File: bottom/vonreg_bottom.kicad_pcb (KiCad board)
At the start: 2 copper layers, 68.6 x 83.6 mm, 8 parts, among them J1 AudioJack4, T1 SW_Push, T2 SW_Push, T3 SW_Push

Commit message: Routing done, hopefully
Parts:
- J1: footprint keebio:TRRS-PJ-320A-dual -> Connector_Audio:TRRS-PJ-320A-dual
- T1, T2, T3: footprint Button_Switch_Keyboard:SW_Cherry_MX_1.00u_PCB -> Button_Switch_Keyboard:Kailh_socket_MX_optional_reversible
- moved T3 5.12 mm to (101.1, 108.3)
- moved T1 5.12 mm to (61.1, 108.3)
- moved T2 5.12 mm to (81.1, 108.3)
- moved J1 0.85 mm to (77.0, 37.2)
- moved BlackPill_reversed1 0.18 mm to (63.1, 38.0)
- gave numbers to parts that had none: 2
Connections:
- BlackPill1 pad 1: K1 -> K14
- BlackPill1 pad 11: K6 -> K2
- BlackPill1 pad 12: K7 -> K15
- BlackPill1 pad 13: K8 -> K9
- BlackPill1 pad 14: K9 -> K12
- BlackPill1 pad 15: K10 -> T3
- BlackPill1 pad 16: K11 -> T2
- BlackPill1 pad 17: K12 -> T1
- BlackPill1 pad 2: K2 -> K13
- BlackPill1 pad 20: 3V3 -> unconnected-(BlackPill1-Pad20)
- BlackPill1 pad 28: TX1 -> K6
- BlackPill1 pad 3: K3 -> TX1
- BlackPill1 pad 30: T3 -> K3
- BlackPill1 pad 31: T2 -> K8
- BlackPill1 pad 32: T1 -> K11
- BlackPill1 pad 33: K15 -> K7
- BlackPill1 pad 34: K14 -> K10
- BlackPill1 pad 35: K13 -> K4
- BlackPill1 pad 4: K4 -> K1
- BlackPill_reversed1 pad 1: K1 -> K14
- BlackPill_reversed1 pad 11: K6 -> K2
- BlackPill_reversed1 pad 12: K7 -> K15
- BlackPill_reversed1 pad 13: K8 -> K9
- BlackPill_reversed1 pad 14: K9 -> K12
- BlackPill_reversed1 pad 15: K10 -> T3
- BlackPill_reversed1 pad 16: K11 -> T2
- BlackPill_reversed1 pad 17: K12 -> T1
- BlackPill_reversed1 pad 2: K2 -> K13
- BlackPill_reversed1 pad 20: 3V3 -> unconnected-(BlackPill_reversed1-Pad20)
- BlackPill_reversed1 pad 28: TX1 -> K6
- BlackPill_reversed1 pad 3: K3 -> TX1
- BlackPill_reversed1 pad 30: T3 -> K3
- BlackPill_reversed1 pad 31: T2 -> K8
- BlackPill_reversed1 pad 32: T1 -> K11
- BlackPill_reversed1 pad 33: K15 -> K7
- BlackPill_reversed1 pad 34: K14 -> K10
- BlackPill_reversed1 pad 35: K13 -> K4
- BlackPill_reversed1 pad 4: K4 -> K1
- PinsBottomA1 pad 1: K1 -> unconnected-(PinsBottomA1-Pad1)
- PinsBottomA1 pad 10: K10 -> K7
- PinsBottomA1 pad 2: K2 -> K14
- PinsBottomA1 pad 3: K3 -> unconnected-(PinsBottomA1-Pad3)
- PinsBottomA1 pad 4: K4 -> K13
- PinsBottomA1 pad 5: K5 -> unconnected-(PinsBottomA1-Pad5)
- PinsBottomA1 pad 6: K6 -> K1
- PinsBottomA1 pad 7: K7 -> unconnected-(PinsBottomA1-Pad7)
- PinsBottomA1 pad 8: K8 -> K4
- PinsBottomA1 pad 9: K9 -> K10
- PinsBottomB1 pad 1: K11 -> K8
- PinsBottomB1 pad 10: GND -> K9
- PinsBottomB1 pad 2: K12 -> K11
- PinsBottomB1 pad 3: K13 -> K5
- PinsBottomB1 pad 4: K14 -> GND
- PinsBottomB1 pad 5: K15 -> K2
- PinsBottomB1 pad 6: unconnected-(PinsBottomB1-Pad6) -> K3
- PinsBottomB1 pad 7: unconnected-(PinsBottomB1-Pad7) -> K15
- PinsBottomB1 pad 8: unconnected-(PinsBottomB1-Pad8) -> K6
- PinsBottomB1 pad 9: unconnected-(PinsBottomB1-Pad9) -> K12
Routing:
- net GND: track 0.00 -> 236.2 mm
- net T3: track 0.00 -> 90.1 mm
- net T2: track 0.00 -> 76.0 mm
- net T1: track 0.00 -> 62.7 mm
- net K6: track 0.00 -> 48.8 mm
- net K11: track 0.00 -> 48.7 mm
- net K3: track 0.00 -> 48.7 mm
- net K8: track 0.00 -> 45.4 mm
- net K9: track 0.00 -> 44.1 mm
- net K7: track 0.00 -> 43.7 mm
- net K4: track 0.00 -> 43.2 mm
- net K13: track 0.00 -> 42.3 mm
- net K5: track 0.00 -> 41.6 mm
- net K15: track 0.00 -> 41.5 mm
- net K2: track 0.00 -> 41.5 mm
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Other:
- outline, holes or cut-outs redrawn

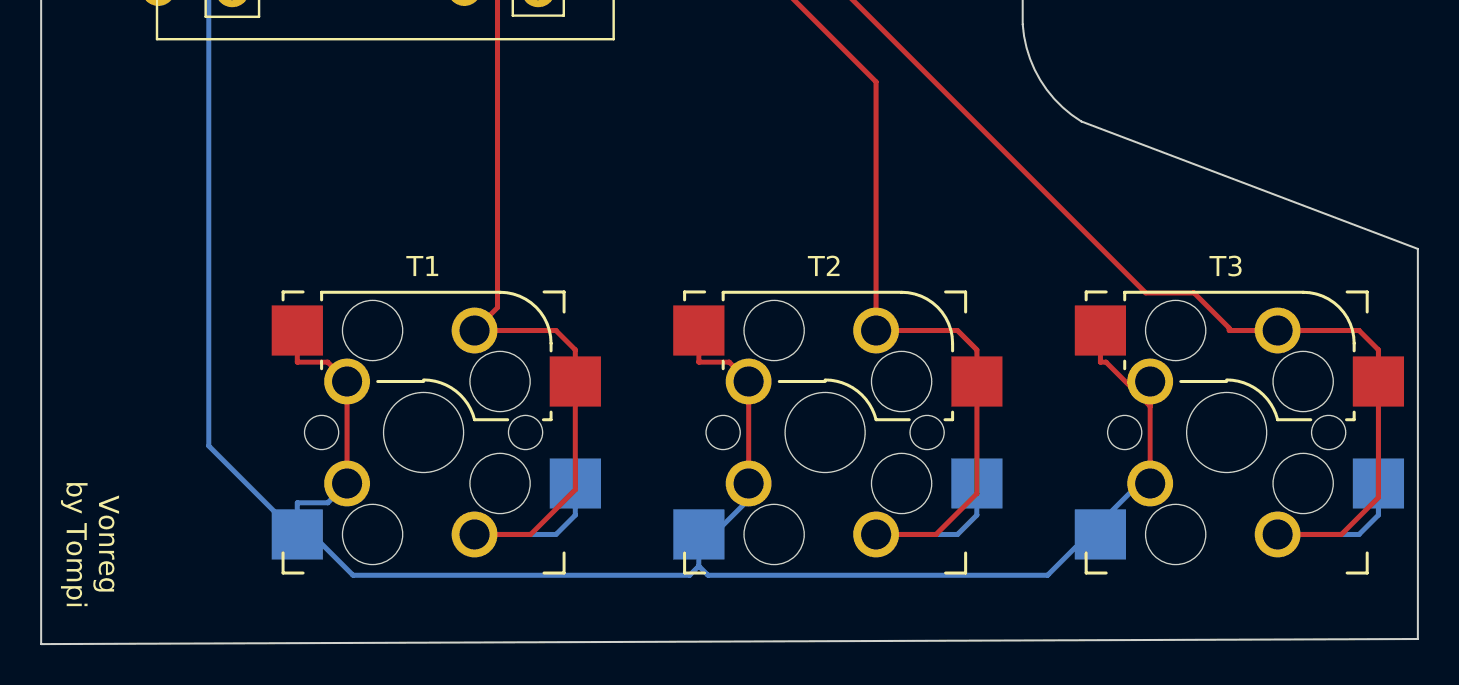
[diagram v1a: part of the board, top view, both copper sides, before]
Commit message: Rounded edge cuts
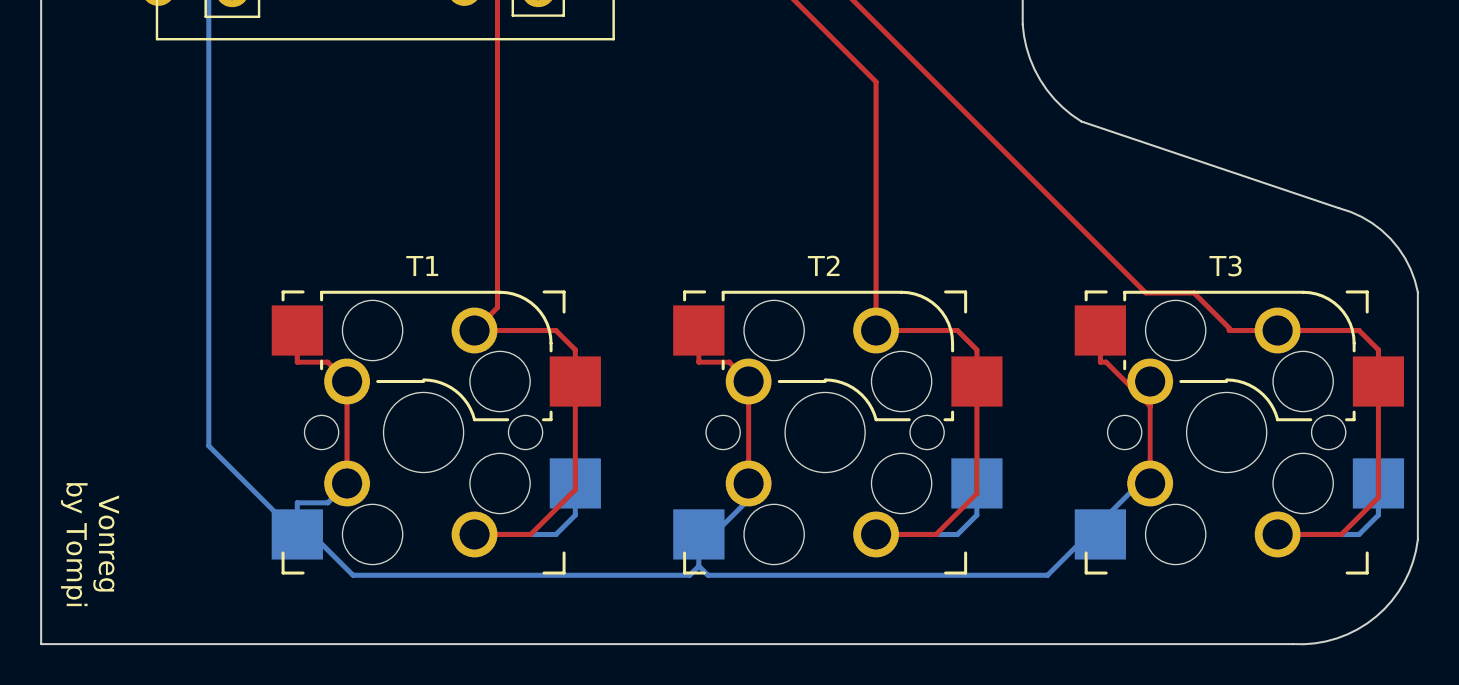
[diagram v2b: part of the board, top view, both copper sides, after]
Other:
- outline, holes or cut-outs redrawn
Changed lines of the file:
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@@
       (outputformat 1)
       (mirror false)
-      (drillshape 1)
+      (drillshape 0)
       (scaleselection 1)
-      (outputdirectory "")
+      (outputdirectory "gerber")
     )
   )
@@
   (gr_line (start 42.037 35.306) (end 84.328 35.306) (layer "Edge.Cuts") (width 0.1))
   (gr_line (start 42.037 118.872) (end 42.037 35.306) (layer "Edge.Cuts") (width 0.1))
-  (gr_line (start 110.617 118.618) (end 42.037 118.872) (layer "Edge.Cuts") (width 0.1))
+  (gr_line (start 104.394 118.872) (end 42.037 118.872) (layer "Edge.Cuts") (width 0.1))
   (gr_line (start 90.932 40.386) (end 90.932 88) (layer "Edge.Cuts") (width 0.1))
-  (gr_line (start 110.617 99.187) (end 110.617 118.618) (layer "Edge.Cuts") (width 0.1))
+  (gr_arc (start 106.68 97.155) (mid 109.256167 98.679662) (end 110.617 101.346) (layer "Edge.Cuts") (width 0.1))
+  (gr_arc (start 110.617 113.665) (mid 108.539478 117.50423) (end 104.394 118.872) (layer "Edge.Cuts") (width 0.1))
+  (gr_line (start 110.617 101.346) (end 110.617 113.665) (layer "Edge.Cuts") (width 0.1))
   (gr_arc (start 93.853 92.837) (mid 91.805949 90.772711) (end 90.932 88) (layer "Edge.Cuts") (width 0.1))
   (gr_arc (start 84.328 35.306) (mid 88.511705 36.699783) (end 90.932 40.386) (layer "Edge.Cuts") (width 0.1))
-  (gr_line (start 93.853 92.837) (end 110.617 99.187) (layer "Edge.Cuts") (width 0.1))
+  (gr_line (start 93.853 92.837) (end 106.68 97.155) (layer "Edge.Cuts") (width 0.1))
   (gr_text "3V3 Here" (at 57.15 83.693) (layer "B.SilkS")
     (effects (font (size 1 1) (thickness 0.15)) (justify mirror))

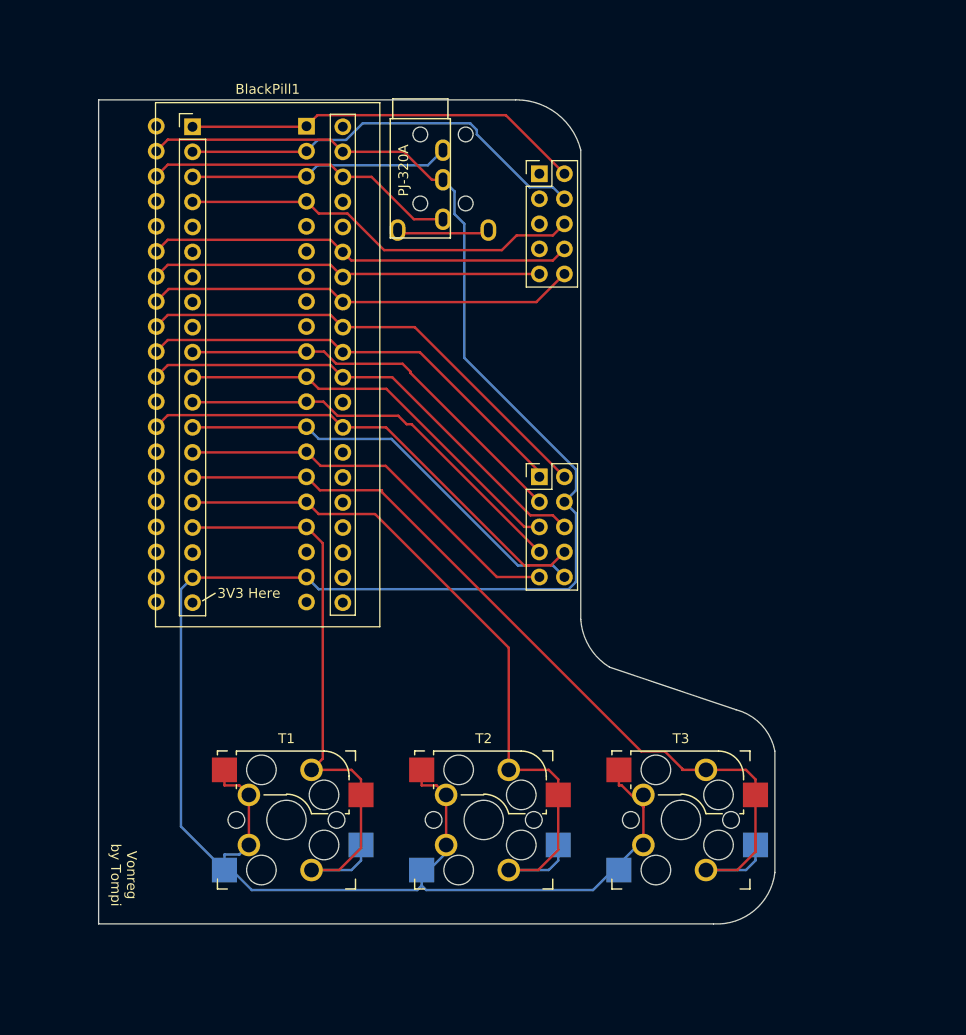
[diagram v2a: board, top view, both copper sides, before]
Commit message: Ground pour and buzzer
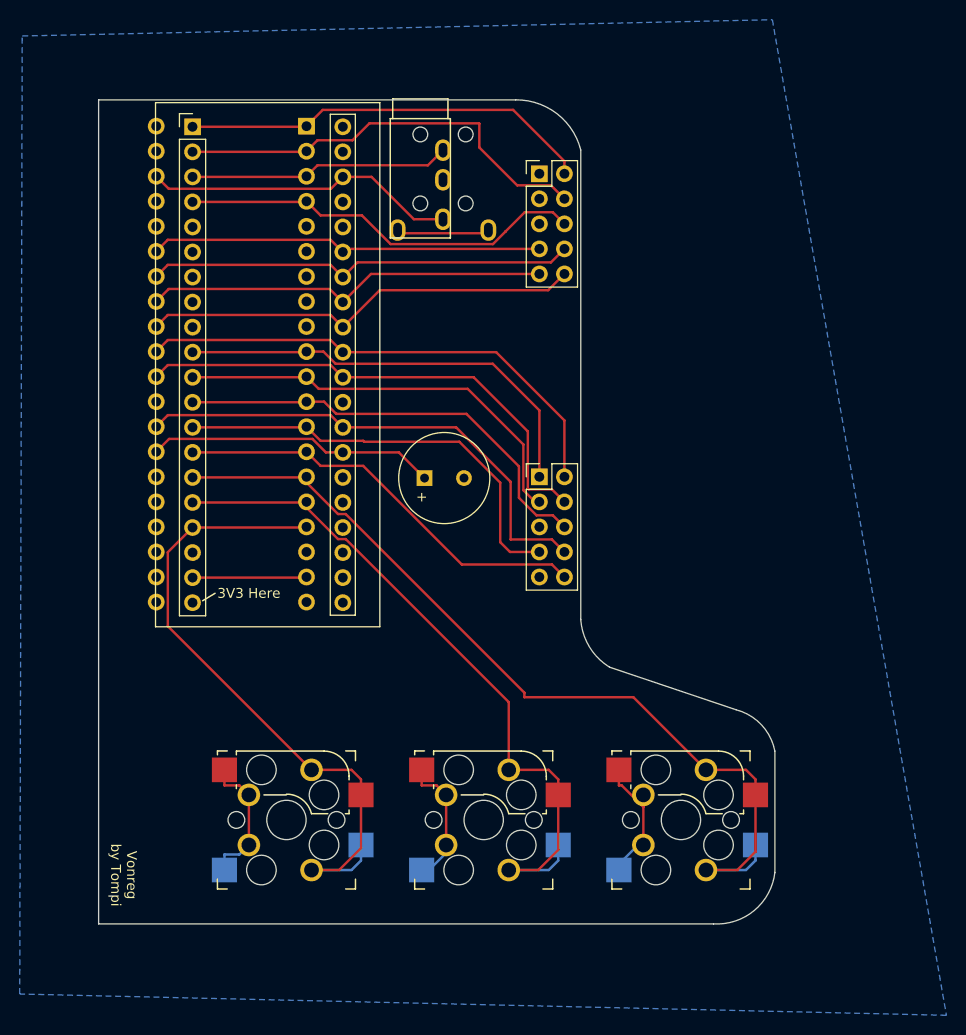
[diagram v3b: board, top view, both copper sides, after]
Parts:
- added BZ1: Buzzer, Buzzer_Beeper:MagneticBuzzer_PUI_AT-0927-TT-6-R, F.Cu at (75.1, 73.7)
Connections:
- BlackPill1 pad 1: K14 -> K1
- BlackPill1 pad 10: K5 -> K2
- BlackPill1 pad 11: K2 -> K8
- BlackPill1 pad 12: K15 -> K12
- BlackPill1 pad 14: K12 -> K3
- BlackPill1 pad 2: K13 -> K4
- BlackPill1 pad 27: unconnected-(BlackPill1-Pad27) -> BUZZER
- BlackPill1 pad 30: K3 -> K15
- BlackPill1 pad 31: K8 -> K5
- BlackPill1 pad 33: K7 -> K14
- BlackPill1 pad 34: K10 -> K13
- BlackPill1 pad 35: K4 -> K10
- BlackPill1 pad 4: K1 -> K7
- BlackPill_reversed1 pad 1: K14 -> K1
- BlackPill_reversed1 pad 10: K5 -> K2
- BlackPill_reversed1 pad 11: K2 -> K8
- BlackPill_reversed1 pad 12: K15 -> K12
- BlackPill_reversed1 pad 14: K12 -> K3
- BlackPill_reversed1 pad 2: K13 -> K4
- BlackPill_reversed1 pad 27: unconnected-(BlackPill_reversed1-Pad27) -> BUZZER
- BlackPill_reversed1 pad 30: K3 -> K15
- BlackPill_reversed1 pad 31: K8 -> K5
- BlackPill_reversed1 pad 33: K7 -> K14
- BlackPill_reversed1 pad 34: K10 -> K13
- BlackPill_reversed1 pad 35: K4 -> K10
- BlackPill_reversed1 pad 4: K1 -> K7
- PinsBottomA1 pad 1: unconnected-(PinsBottomA1-Pad1) -> GND
- PinsBottomA1 pad 10: K7 -> K11
- PinsBottomA1 pad 2: K14 -> K1
- PinsBottomA1 pad 4: K13 -> K4
- PinsBottomA1 pad 6: K1 -> K7
- PinsBottomA1 pad 7: unconnected-(PinsBottomA1-Pad7) -> K10
- PinsBottomA1 pad 8: K4 -> K13
- PinsBottomA1 pad 9: K10 -> K14
- PinsBottomB1 pad 1: K8 -> K2
- PinsBottomB1 pad 10: K9 -> K3
- PinsBottomB1 pad 2: K11 -> K5
- PinsBottomB1 pad 3: K5 -> K8
- PinsBottomB1 pad 4: GND -> K15
- PinsBottomB1 pad 5: K2 -> unconnected-(PinsBottomB1-Pad5)
- PinsBottomB1 pad 6: K3 -> K12
- PinsBottomB1 pad 7: K15 -> K9
- PinsBottomB1 pad 9: K12 -> unconnected-(PinsBottomB1-Pad9)
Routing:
- net GND: track 236.2 -> 54.1 mm
- net BUZZER: track 0.00 -> 29.6 mm
- net K15: track 41.5 -> 51.0 mm
- net K5: track 41.6 -> 51.0 mm
- net T1: track 62.7 -> 68.6 mm
- net K3: track 48.7 -> 43.0 mm
- net K12: track 40.5 -> 44.9 mm
- net K11: track 48.7 -> 44.6 mm
- net K2: track 41.5 -> 44.4 mm
- net T2: track 76.0 -> 73.2 mm
- net K7: track 43.7 -> 41.4 mm
- net K6: track 48.8 -> 51.1 mm
- net K8: track 45.4 -> 43.2 mm
- net K13: track 42.3 -> 43.6 mm
- net K1: track 40.9 -> 41.9 mm
- added copper zone on B.Cu, net GND
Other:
- board text added: "+"
